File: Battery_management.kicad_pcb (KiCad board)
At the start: 2 copper layers, 11 parts, among them IC1 MCP73834-FCI_UN

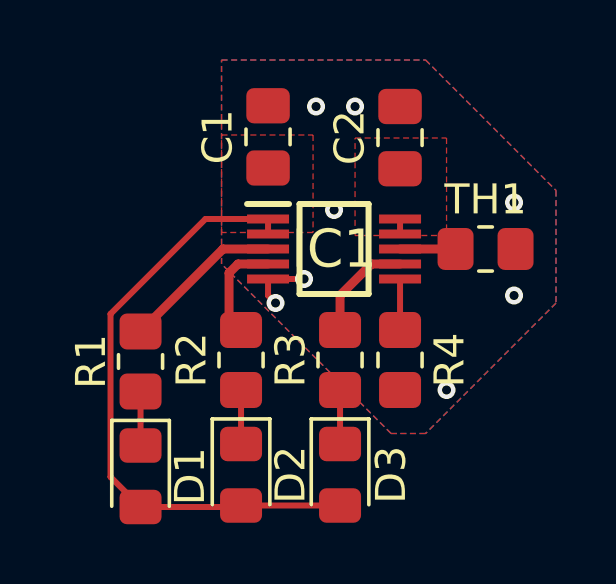
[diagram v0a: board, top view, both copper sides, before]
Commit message: Add 0402 version
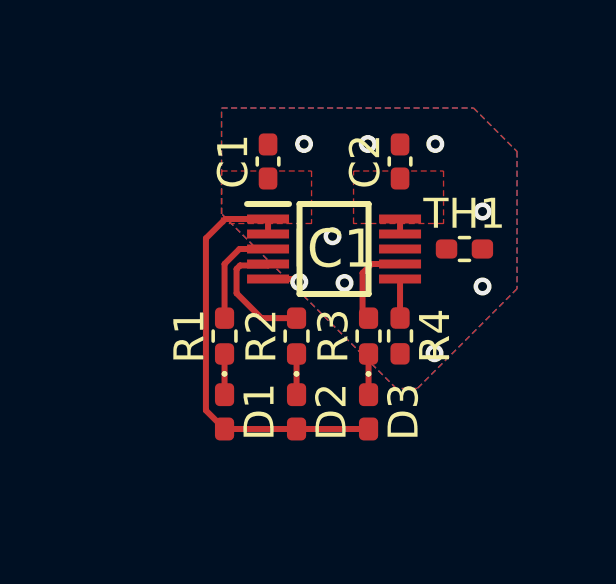
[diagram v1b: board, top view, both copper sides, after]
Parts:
- C1, C2: footprint Capacitor_SMD:C_0805_2012Metric_Pad1.18x1.45mm_HandSolder -> Capacitor_SMD:C_0402_1005Metric_Pad0.74x0.62mm_HandSolder
- D1, D2, D3: footprint LED_SMD:LED_0805_2012Metric_Pad1.15x1.40mm_HandSolder -> LED_SMD:LED_0402_1005Metric_Pad0.77x0.64mm_HandSolder
- R1, R2, R3, R4, TH1: footprint Resistor_SMD:R_0805_2012Metric_Pad1.20x1.40mm_HandSolder -> Resistor_SMD:R_0402_1005Metric_Pad0.72x0.64mm_HandSolder
- moved D1 3.53 mm to (174.2, 90.3)
- moved R1 2.93 mm to (174.2, 87.8)
- moved D2 2.80 mm to (176.6, 90.3)
- moved D3 2.30 mm to (179.0, 90.3)
- moved R2 2.01 mm to (176.6, 87.8)
- moved R3 1.24 mm to (179.0, 87.8)
- moved C1 0.82 mm to (175.7, 81.9)
- moved R4 0.80 mm to (180.1, 87.7)
- moved C2 0.80 mm to (180.1, 81.9)
- moved TH1 0.70 mm to (182.2, 84.8)
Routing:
- net +5V: track 20.6 -> 14.2 mm
- net Net-(IC1-STAT1): track 5.39 -> 3.46 mm
- net Net-(IC1-THERM): track 1.85 -> 0.00 mm
- net GND: track 2.10 -> 1.08 mm, vias 8 -> 9
- net Net-(IC1-STAT2): track 3.49 -> 4.30 mm
- net Net-(IC1-~{_PG(TE)}): track 3.59 -> 2.96 mm
